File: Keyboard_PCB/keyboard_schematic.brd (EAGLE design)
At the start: 487.7 x 175.3 mm, 266 parts, among them IC1 LMV321M5, M2 KEYSWITCH-RGBSMDLED-ALPSMX-1U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, M3 KEYSWITCH-RGBSMDLED-ALPSMX-1U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, M4 KEYSWITCH-RGBSMDLED-ALPSMX-1U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, M5 KEYSWITCH-RGBSMDLED-ALPSMX-1U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, M6 KEYSWITCH-RGBSMDLED-ALPSMX-1U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, T1 BC846, Y2 CRYSTAL-GROUNDEDSMD-3.2X2.5

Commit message: Updated Schematics and boards
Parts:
- removed IC2: (no value), controller-micro_atmel_jd:QFN64
- removed U$2: PCB_USB_CDS_1, USB_pcb_connectors:USB_TYPE_C_DS_1
- added IC3: (no value), controller-micro_atmel_jd:TQFP64
- added J1: 1-2295018-2, 1-2295018-2:TE_1-2295018-2
- T1: value BC846 -> (none); device transistor:SOT23 -> transistor:SOT23-EBC
- moved C7 430.1 mm to (370.1, 134.4), flipped to the bottom, turned to 90 degrees
- moved R1 408.4 mm to (348.7, 132.3), flipped to the bottom, turned to 90 degrees
- moved C3 405.0 mm to (355.9, 134.4), flipped to the bottom, turned to 90 degrees
- moved S1 403.3 mm to (334.3, 160.3), flipped to the bottom, turned to 180 degrees
- moved C4 402.9 mm to (359.4, 134.4), flipped to the bottom, turned to 90 degrees
- moved R3 402.6 mm to (348.7, 145.0), flipped to the bottom, turned to 90 degrees
- moved R4 400.9 mm to (348.7, 149.1), flipped to the bottom, turned to 90 degrees
- moved C5 400.8 mm to (363.0, 134.4), flipped to the bottom, turned to 90 degrees
- moved C6 398.7 mm to (366.5, 134.4), flipped to the bottom, turned to 90 degrees
- moved C8 392.7 mm to (337.3, 137.7), flipped to the bottom
- moved R8 390.9 mm to (310.9, 158.5), flipped to the bottom, turned to 270 degrees
- moved T1 388.5 mm to (302.3, 156.0), flipped to the bottom, turned to 90 degrees
- moved R5 385.2 mm to (324.8, 158.0), flipped to the bottom, turned to 270 degrees
- moved R6 379.0 mm to (322.4, 158.0), flipped to the bottom, turned to 90 degrees
- moved C2 377.4 mm to (327.9, 124.7), flipped to the bottom, turned to 90 degrees
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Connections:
- removed net COL11: EQUAL2.ALPS1, EQUAL2.MX1, KP_9.ALPS1, KP_9.MX1, KP_ASTERISK.ALPS1, KP_ASTERISK.MX1, KP_DASH.ALPS1, KP_DASH.MX1, NEXTSONG.ALPS1, NEXTSONG.MX1, PAUSEPLAY.ALPS1, PAUSEPLAY.MX1
- removed net ROW1.1: DF1.C, DF11.C, DF3.C, DF5.C, DF7.C, DF9.C, DM6.C, DNEXTSONG1.C, DPAUSE.C, DPAUSEPLAY.C, DSCROLLLOCK.C, DVOLUMEUP.C
- removed net ROW1.2: DBACKSONG.C, DESC.C, DF10.C, DF12.C, DF2.C, DF4.C, DF6.C, DF8.C, DLOCK.C, DNEXTSONG.C, DPRTSC.C, DVOLUMNEDOWN.C
- removed net ROW2.1: D1.C, D3.C, D5.C, D7.C, D9.C, DBACKSPACE.C, DDASH.C, DHOME.C, DKP_DASH.C, DKP_SLASH.C, DM5.C
- removed net ROW2.2: D0.C, D2.C, D4.C, D6.C, D8.C, DEQUAL.C, DGRAVE.C, DINSERT.C, DKP_ASTERISK.C, DNUMLOCK.C, DPGUP.C, DUNDERSCORE.C
- removed net ROW3.1: DBACKSLASH.C, DE.C, DEND.C, DEQUAL2.C, DKP_8.C, DLBRACKET.C, DM4.C, DO.C, DQ.C, DT.C, DU.C
- removed net ROW3.2: DDELETE.C, DI.C, DKP_5.C, DKP_7.C, DKP_9.C, DP.C, DPGDN.C, DR.C, DRBRACKET.C, DTAB.C, DW.C, DY.C
- removed net ROW4.1: DA.C, DCTRL2.C, DD.C, DG.C, DJ.C, DKP_4.C, DKP_6.C, DKP_62.C, DL.C, DM3.C, DQUOTE.C
- removed net ROW4.2: DCAPSLOCK.C, DENTER.C, DENTER2.C, DF.C, DH.C, DK.C, DKP_52.C, DS.C, DSEMICOLON.C, DUP.C
- removed net ROW5.1: DB.C, DC.C, DKP_2.C, DLEFT.C, DM.C, DM2.C, DMENU.C, DPERIOD.C, DZ.C
- removed net ROW5.2: DCOMMA.C, DDELETE2.C, DKP_1.C, DKP_3.C, DN.C, DRIGHT.C, DSHIFT.C, DSHIFT2.C, DSLASH.C, DV.C, DX.C
- removed net ROW6.1: DALT.C, DALT2.C, DBACKSPACE_1.C, DCTRL.C, DDOWN.C, DKP_0.C, DKP_DEL.C, DM1.C, DSPACE.C, DWIN.C, DWIN2.C
- new net COL13: 0.ALPS1, 0.MX1, F10.ALPS1, F10.MX1, P.ALPS1, P.MX1, SEMICOLON.ALPS1, SEMICOLON.MX1, SLASH.ALPS1, SLASH.MX1, WIN2.ALPS1, WIN2.MX1
- new net COL14: DASH.ALPS1, DASH.MX1, F11.ALPS1, F11.MX1, LBRACKET.ALPS1, LBRACKET.MX1, MENU.ALPS1, MENU.MX1, QUOTE.ALPS1, QUOTE.MX1
- new net COL15: EQUAL.ALPS1, EQUAL.MX1, F12.ALPS1, F12.MX1, RBRACKET.ALPS1, RBRACKET.MX1
- new net COL16: VOLUMEUP.ALPS1, VOLUMEUP.MX1
- new net COL17: BACKSLASH.ALPS1, BACKSLASH.MX1, BACKSPACE.ALPS1, BACKSPACE.MX1, CTRL2.ALPS1, CTRL2.MX1, ENTER.ALPS1, ENTER.MX1, SHIFT2.ALPS1, SHIFT2.MX1, VOLUMNEDOWN.ALPS1, VOLUMNEDOWN.MX1
- new net COL18: DELETE.ALPS1, DELETE.MX1, INSERT.ALPS1, INSERT.MX1, LEFT.ALPS1, LEFT.MX1, PRTSC.ALPS1, PRTSC.MX1
- new net COL19: DOWN.ALPS1, DOWN.MX1, END.ALPS1, END.MX1, HOME.ALPS1, HOME.MX1, SCROLLLOCK.ALPS1, SCROLLLOCK.MX1, UP.ALPS1, UP.MX1
- new net COL20: PAUSE.ALPS1, PAUSE.MX1, PGDN.ALPS1, PGDN.MX1, PGUP.ALPS1, PGUP.MX1, RIGHT.ALPS1, RIGHT.MX1
- new net COL21: BACKSONG.ALPS1, BACKSONG.MX1, KP_0.ALPS1, KP_0.MX1, KP_1.ALPS1, KP_1.MX1, KP_4.ALPS1, KP_4.MX1, KP_7.ALPS1, KP_7.MX1, NUMLOCK.ALPS1, NUMLOCK.MX1
- new net COL22: KP_2.ALPS1, KP_2.MX1, KP_52.ALPS1, KP_52.MX1, KP_8.ALPS1, KP_8.MX1, KP_SLASH.ALPS1, KP_SLASH.MX1, PAUSEPLAY.ALPS1, PAUSEPLAY.MX1
- new net COL23: KP_3.ALPS1, KP_3.MX1, KP_6.ALPS1, KP_6.MX1, KP_9.ALPS1, KP_9.MX1, KP_ASTERISK.ALPS1, KP_ASTERISK.MX1, KP_DEL.ALPS1, KP_DEL.MX1, NEXTSONG.ALPS1, NEXTSONG.MX1
- new net COL24: ENTER2.ALPS1, ENTER2.MX1, EQUAL2.ALPS1, EQUAL2.MX1, KP_DASH.ALPS1, KP_DASH.MX1, RANDSONG.ALPS1, RANDSONG.MX1
- new net COL25: BACKSPACE_1.ALPS1, BACKSPACE_1.MX1, KP_5.ALPS1, KP_5.MX1, KP_62.ALPS1, KP_62.MX1, KP_DELETE2.ALPS1, KP_DELETE2.MX1, LOCK.ALPS1, LOCK.MX1, UNDERSCORE.ALPS1, UNDERSCORE.MX1
- new net LED1: M6.DIN
- new net LED2: M5.DIN
- new net LED3: M4.DIN
- new net LED4: M3.DIN
- new net LED5: M2.DIN
- new net LED6: CTRL1.DIN
- new net N$107: ESC.DIN, M6.DOUT
- new net N$118: ESC.DOUT, F1.DIN
- new net N$119: F1.DOUT, F2.DIN
- new net N$121: F2.DOUT, F3.DIN
- new net N$122: F3.DOUT, F4.DIN
- new net N$123: F4.DOUT, F5.DIN
- new net N$124: F5.DOUT, F6.DIN
- new net N$132: F6.DOUT, F7.DIN
- new net N$133: F7.DOUT, F8.DIN
- new net N$134: F8.DOUT, F9.DIN
- new net N$135: F10.DIN, F9.DOUT
- new net N$136: F10.DOUT, F11.DIN
- new net N$137: F11.DOUT, F12.DIN
- new net N$138: F12.DOUT, VOLUMEUP.DIN
- new net N$139: VOLUMEUP.DOUT, VOLUMNEDOWN.DIN
- new net N$140: PRTSC.DIN, VOLUMNEDOWN.DOUT
- new net N$141: PRTSC.DOUT, SCROLLLOCK.DIN
- new net N$142: PAUSE.DIN, SCROLLLOCK.DOUT
- new net N$143: BACKSONG.DIN, PAUSE.DOUT
- new net N$144: BACKSONG.DOUT, PAUSEPLAY.DIN
- new net N$145: NEXTSONG.DIN, PAUSEPLAY.DOUT
- new net N$146: NEXTSONG.DOUT, RANDSONG.DIN
- new net N$147: LOCK.DIN, RANDSONG.DOUT
- new net N$148: IC3.50
- new net N$149: GRAVE.DIN, M5.DOUT
- new net N$150: 1.DIN, GRAVE.DOUT
- new net N$151: 1.DOUT, 2.DIN
- new net N$152: 2.DOUT, 3.DIN
- new net N$153: 3.DOUT, 4.DIN
- new net N$154: 4.DOUT, 5.DIN
- new net N$155: 5.DOUT, 6.DIN
- new net N$156: 6.DOUT, 7.DIN
- new net N$157: 7.DOUT, 8.DIN
- new net N$158: 8.DOUT, 9.DIN
- new net N$159: 0.DIN, 9.DOUT
- new net N$160: 0.DOUT, DASH.DIN
- new net N$161: DASH.DOUT, EQUAL.DIN
- new net N$162: IC3.49
- new net N$163: BACKSPACE.R-, EQUAL.DOUT
- new net N$164: BACKSPACE.G-, INSERT.DIN
- new net N$165: HOME.DIN, INSERT.DOUT
- new net N$166: HOME.DOUT, PGUP.DIN
- new net N$167: NUMLOCK.DIN, PGUP.DOUT
- new net N$168: KP_SLASH.DIN, NUMLOCK.DOUT
- new net N$169: KP_ASTERISK.DIN, KP_SLASH.DOUT
- new net N$170: KP_ASTERISK.DOUT, KP_DASH.DIN
- new net N$171: KP_DASH.DOUT, UNDERSCORE.DIN
- new net N$172: M4.DOUT, TAB.DIN
- new net N$173: Q.DIN, TAB.DOUT
- new net N$174: Q.DOUT, W.DIN
- new net N$175: E.DIN, W.DOUT
- new net N$176: E.DOUT, R.DIN
- new net N$177: R.DOUT, T.DIN
- new net N$178: T.DOUT, Y.DIN
- new net N$179: U.DIN, Y.DOUT
- new net N$180: I.DIN, U.DOUT
- new net N$181: I.DOUT, O.DIN
- new net N$182: O.DOUT, P.DIN
- new net N$183: LBRACKET.DIN, P.DOUT
- new net N$184: LBRACKET.DOUT, RBRACKET.DIN
- new net N$185: BACKSLASH.DIN, RBRACKET.DOUT
- new net N$186: IC3.48
- new net N$187: BACKSLASH.DOUT, DELETE.DIN
- new net N$188: DELETE.DOUT, END.DIN
- new net N$189: END.DOUT, PGDN.DIN
- new net N$190: KP_7.DIN, PGDN.DOUT
- new net N$191: KP_7.DOUT, KP_8.DIN
- new net N$192: KP_8.DOUT, KP_9.DIN
- new net N$193: EQUAL2.DIN, KP_9.DOUT
- new net N$194: EQUAL2.DOUT, KP_5.DIN
- new net N$195: CAPSLOCK.DIN, M3.DOUT
- new net N$196: A.DIN, CAPSLOCK.DOUT
- new net N$197: A.DOUT, S.DIN
- new net N$198: D.DIN, S.DOUT
- new net N$199: D.DOUT, F.DIN
- new net N$200: F.DOUT, G.DIN
- new net N$201: G.DOUT, H.DIN
- new net N$202: H.DOUT, J.DIN
- new net N$203: J.DOUT, K.DIN
- new net N$204: K.DOUT, L.DIN
- new net N$205: L.DOUT, SEMICOLON.DIN
- new net N$206: QUOTE.DIN, SEMICOLON.DOUT
- new net N$207: ENTER.R-, QUOTE.DOUT
- new net N$208: ENTER.G-, KP_4.DIN
- new net N$209: ENTER2.DIN, KP_3.DOUT
- new net N$210: KP_4.DOUT, KP_52.DIN
- new net N$211: KP_52.DOUT, KP_6.DIN
- new net N$212: KP_6.DOUT, KP_62.DIN
- new net N$213: IC3.47
- new net N$214: M2.DOUT, SHIFT.R-
- new net N$215: SHIFT.G-, Z.DIN
- new net N$216: X.DIN, Z.DOUT
- new net N$217: C.DIN, X.DOUT
- new net N$218: C.DOUT, V.DIN
- new net N$219: B.DIN, V.DOUT
- new net N$220: B.DOUT, N.DIN
- new net N$221: M.DIN, N.DOUT
- new net N$222: COMMA.DIN, M.DOUT
- new net N$223: COMMA.DOUT, PERIOD.DIN
- new net N$224: PERIOD.DOUT, SLASH.DIN
- new net N$225: SHIFT2.R-, SLASH.DOUT
- new net N$226: IC3.46
- new net N$227: KP_1.DOUT, KP_2.DIN
- new net N$228: KP_2.DOUT, KP_3.DIN
- new net N$229: ENTER2.DOUT, KP_DELETE2.DIN
- new net N$230: KP_1.DIN, SHIFT2.G-
- new net N$231: IC3.45
- new net N$232: CTRL.DIN, CTRL1.DOUT
- new net N$233: CTRL.DOUT, WIN.DIN
- new net N$234: ALT.DIN, WIN.DOUT
- new net N$235: ALT.DOUT, SPACE.R-
- new net N$236: IC3.44
- new net N$238: ALT2.DIN, SPACE.G-
- new net N$239: J1.B9
- new net N$242: ALT2.DOUT, WIN2.DIN
- new net N$243: MENU.DIN, WIN2.DOUT
- new net N$245: CTRL2.DIN, MENU.DOUT
- new net N$246: CTRL2.DOUT, LEFT.DIN
- new net N$247: KP_0.R-
- new net N$248: KP_0.G-, KP_DEL.DIN
- new net N$249: BACKSPACE_1.DIN, KP_DEL.DOUT
- new net N$250: DOWN.DIN, LEFT.DOUT
- new net N$251: DOWN.DOUT, RIGHT.DIN
- new net N$252: RIGHT.DOUT
- new net ROW1: DBACKSONG.C, DESC.C, DF1.C, DF10.C, DF11.C, DF12.C, DF2.C, DF3.C, DF4.C, DF5.C, DF6.C, DF7.C, DF8.C, DF9.C, DLOCK.C, DM6.C, DNEXTSONG.C, DNEXTSONG1.C, DPAUSE.C, DPAUSEPLAY.C, DPRTSC.C, DSCROLLLOCK.C, DVOLUMEUP.C, DVOLUMNEDOWN.C
- new net ROW2: D0.C, D1.C, D2.C, D3.C, D4.C, D5.C, D6.C, D7.C, D8.C, D9.C, DBACKSPACE.C, DDASH.C, DEQUAL.C, DGRAVE.C, DHOME.C, DINSERT.C, DKP_ASTERISK.C, DKP_DASH.C, DKP_SLASH.C, DM5.C, DNUMLOCK.C, DPGUP.C, DUNDERSCORE.C
- new net ROW3: DBACKSLASH.C, DDELETE.C, DE.C, DEND.C, DEQUAL2.C, DI.C, DKP_5.C, DKP_7.C, DKP_8.C, DKP_9.C, DLBRACKET.C, DM4.C, DO.C, DP.C, DPGDN.C, DQ.C, DR.C, DRBRACKET.C, DT.C, DTAB.C, DU.C, DW.C, DY.C
- new net ROW4: DA.C, DCAPSLOCK.C, DD.C, DENTER.C, DF.C, DG.C, DH.C, DJ.C, DK.C, DKP_4.C, DKP_52.C, DKP_6.C, DKP_62.C, DL.C, DM3.C, DQUOTE.C, DS.C, DSEMICOLON.C
- new net ROW5: DB.C, DC.C, DCOMMA.C, DDELETE2.C, DENTER2.C, DKP_1.C, DKP_2.C, DKP_3.C, DM.C, DM2.C, DN.C, DPERIOD.C, DSHIFT.C, DSHIFT2.C, DSLASH.C, DUP.C, DV.C, DX.C, DZ.C
- new net ROW6: DALT.C, DALT2.C, DBACKSPACE_1.C, DCTRL2.C, DDOWN.C, DKP_0.C, DKP_DEL.C, DLEFT.C, DM1.C, DMENU.C, DRIGHT.C, DSPACE.C, DWIN.C, DWIN2.C
- net +5V: now also IC3.21, IC3.52, IC3.62, IC3.64, J1.A4, J1.A9, J1.B4, T1.C; no longer IC2.21, IC2.52, IC2.62, IC2.64, T1.3, U$2.A4, U$2.A9, U$2.B4, U$2.B9
- net CC1: now also IC1.1, J1.A5, R6.2; no longer R5.1, U$2.A5
- net CC2: now also J1.B5, R5.1; no longer IC1.1, R6.2, U$2.B5
- net COL1: no longer CAPSLOCK.ALPS1, CAPSLOCK.MX1, ESC.ALPS1, ESC.MX1, GRAVE.ALPS1, GRAVE.MX1, SHIFT.ALPS1, SHIFT.MX1, TAB.ALPS1, TAB.MX1
- net COL10: now also 8.ALPS1, 8.MX1, COMMA.ALPS1, COMMA.MX1, F8.ALPS1, F8.MX1, I.ALPS1, I.MX1, K.ALPS1, K.MX1; no longer BACKSONG.ALPS1, BACKSONG.MX1, ENTER2.ALPS1, ENTER2.MX1, KP_3.ALPS1, KP_3.MX1, KP_6.ALPS1, KP_6.MX1, KP_7.ALPS1, KP_7.MX1, KP_8.ALPS1, KP_8.MX1, KP_DEL.ALPS1, KP_DEL.MX1, KP_SLASH.ALPS1, KP_SLASH.MX1, NUMLOCK.ALPS1, NUMLOCK.MX1, PAUSE.ALPS1, PAUSE.MX1
- net COL12: now also 9.ALPS1, 9.MX1, ALT2.ALPS1, ALT2.MX1, F9.ALPS1, F9.MX1, L.ALPS1, L.MX1, O.ALPS1, O.MX1, PERIOD.ALPS1, PERIOD.MX1; no longer BACKSPACE_1.ALPS1, BACKSPACE_1.MX1, KP_5.ALPS1, KP_5.MX1, KP_62.ALPS1, KP_62.MX1, KP_DELETE2.ALPS1, KP_DELETE2.MX1, LOCK.ALPS1, LOCK.MX1, RANDSONG.ALPS1, RANDSONG.MX1, UNDERSCORE.ALPS1, UNDERSCORE.MX1
- net COL2: now also CAPSLOCK.ALPS1, CAPSLOCK.MX1, ESC.ALPS1, ESC.MX1, GRAVE.ALPS1, GRAVE.MX1, SHIFT.ALPS1, SHIFT.MX1, TAB.ALPS1, TAB.MX1; no longer 1.ALPS1, 1.MX1, 2.ALPS1, 2.MX1, A.ALPS1, A.MX1, F1.ALPS1, F1.MX1, F2.ALPS1, F2.MX1, Q.ALPS1, Q.MX1, S.ALPS1, S.MX1, W.ALPS1, W.MX1, X.ALPS1, X.MX1, Z.ALPS1, Z.MX1
- net COL3: now also 1.ALPS1, 1.MX1, A.ALPS1, A.MX1, F1.ALPS1, F1.MX1, Q.ALPS1, Q.MX1, Z.ALPS1, Z.MX1; no longer 3.ALPS1, 3.MX1, 4.ALPS1, 4.MX1, C.ALPS1, C.MX1, D.ALPS1, D.MX1, E.ALPS1, E.MX1, F.ALPS1, F.MX1, F3.ALPS1, F3.MX1, F4.ALPS1, F4.MX1, R.ALPS1, R.MX1, V.ALPS1, V.MX1
- net COL4: now also 2.ALPS1, 2.MX1, F2.ALPS1, F2.MX1, S.ALPS1, S.MX1, W.ALPS1, W.MX1, X.ALPS1, X.MX1; no longer 5.ALPS1, 5.MX1, 6.ALPS1, 6.MX1, B.ALPS1, B.MX1, F5.ALPS1, F5.MX1, F6.ALPS1, F6.MX1, G.ALPS1, G.MX1, H.ALPS1, H.MX1, N.ALPS1, N.MX1, T.ALPS1, T.MX1, Y.ALPS1, Y.MX1
- net COL5: now also 3.ALPS1, 3.MX1, C.ALPS1, C.MX1, D.ALPS1, D.MX1, E.ALPS1, E.MX1, F3.ALPS1, F3.MX1; no longer 7.ALPS1, 7.MX1, 8.ALPS1, 8.MX1, COMMA.ALPS1, COMMA.MX1, F7.ALPS1, F7.MX1, F8.ALPS1, F8.MX1, I.ALPS1, I.MX1, J.ALPS1, J.MX1, K.ALPS1, K.MX1, M.ALPS1, M.MX1, SPACE.ALPS1, SPACE.MX1, U.ALPS1, U.MX1
- net COL6: now also 4.ALPS1, 4.MX1, F.ALPS1, F.MX1, F4.ALPS1, F4.MX1, R.ALPS1, R.MX1, V.ALPS1, V.MX1; no longer 0.ALPS1, 0.MX1, 9.ALPS1, 9.MX1, ALT2.ALPS1, ALT2.MX1, F10.ALPS1, F10.MX1, F9.ALPS1, F9.MX1, L.ALPS1, L.MX1, O.ALPS1, O.MX1, P.ALPS1, P.MX1, PERIOD.ALPS1, PERIOD.MX1, SEMICOLON.ALPS1, SEMICOLON.MX1, SLASH.ALPS1, SLASH.MX1
- net COL7: now also 5.ALPS1, 5.MX1, B.ALPS1, B.MX1, F5.ALPS1, F5.MX1, G.ALPS1, G.MX1, SPACE.ALPS1, SPACE.MX1, T.ALPS1, T.MX1; no longer DASH.ALPS1, DASH.MX1, ENTER.ALPS1, ENTER.MX1, EQUAL.ALPS1, EQUAL.MX1, F11.ALPS1, F11.MX1, F12.ALPS1, F12.MX1, LBRACKET.ALPS1, LBRACKET.MX1, MENU.ALPS1, MENU.MX1, QUOTE.ALPS1, QUOTE.MX1, RBRACKET.ALPS1, RBRACKET.MX1, SHIFT2.ALPS1, SHIFT2.MX1, WIN2.ALPS1, WIN2.MX1
- net COL8: now also 6.ALPS1, 6.MX1, F6.ALPS1, F6.MX1, H.ALPS1, H.MX1, N.ALPS1, N.MX1, Y.ALPS1, Y.MX1; no longer BACKSLASH.ALPS1, BACKSLASH.MX1, BACKSPACE.ALPS1, BACKSPACE.MX1, CTRL2.ALPS1, CTRL2.MX1, DELETE.ALPS1, DELETE.MX1, DOWN.ALPS1, DOWN.MX1, INSERT.ALPS1, INSERT.MX1, LEFT.ALPS1, LEFT.MX1, RIGHT.ALPS1, RIGHT.MX1, UP.ALPS1, UP.MX1, VOLUMEUP.ALPS1, VOLUMEUP.MX1, VOLUMNEDOWN.ALPS1, VOLUMNEDOWN.MX1
- net COL9: now also 7.ALPS1, 7.MX1, F7.ALPS1, F7.MX1, J.ALPS1, J.MX1, M.ALPS1, M.MX1, U.ALPS1, U.MX1; no longer END.ALPS1, END.MX1, HOME.ALPS1, HOME.MX1, KP_0.ALPS1, KP_0.MX1, KP_1.ALPS1, KP_1.MX1, KP_2.ALPS1, KP_2.MX1, KP_4.ALPS1, KP_4.MX1, KP_52.ALPS1, KP_52.MX1, PGDN.ALPS1, PGDN.MX1, PGUP.ALPS1, PGUP.MX1, PRTSC.ALPS1, PRTSC.MX1, SCROLLLOCK.ALPS1, SCROLLLOCK.MX1
- net D+32U: now also IC3.5; no longer IC2.5
- net D+USB: now also J1.B6; no longer U$2.A6
- net D-32U4: now also IC3.4; no longer IC2.4
- net D-USB: now also J1.B7; no longer U$2.A7
- net GND: now also IC3.22, IC3.53, IC3.6, IC3.63, J1.A1, J1.A12, J1.B1, J1.B12, J1.P1_1, J1.P1_2, J1.P2_1, J1.P2_2, J1.P4, J1.P5; no longer IC2.22, IC2.53, IC2.6, IC2.63, U$2.A1, U$2.A12, U$2.B1, U$2.B12
- net LED_VCC: now also T1.E; no longer T1.2
- net N$102: now also IC3.51; no longer CTRL.ALPS2, CTRL.MX2, DCTRL.A
- net N$117: now also T1.B; no longer T1.1
- net PE2: now also IC3.43; no longer IC2.43
- net RESET: now also IC3.20; no longer IC2.20
- net UCAP: now also IC3.7; no longer IC2.7
- net UVCC: now also IC3.3; no longer IC2.3
- net XTAL1: now also IC3.24; no longer IC2.24
- net XTAL2: now also IC3.23; no longer IC2.23
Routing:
- net GND: track 0.00 -> 110.0 mm
- net VCC: track 0.00 -> 17.6 mm
- net +5V: track 0.00 -> 14.4 mm, vias 0 -> 2
- net XTAL2: track 0.00 -> 10.0 mm
- net UCAP: track 0.00 -> 5.84 mm
- net N$116: track 0.00 -> 5.39 mm
- net PE2: track 0.00 -> 4.02 mm
- net XTAL1: track 0.00 -> 3.81 mm
- net N$117: track 0.00 -> 1.27 mm

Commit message: Updated board
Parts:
- moved C7 40.7 mm to (330.9, 145.4), turned to 270 degrees
- moved C6 35.3 mm to (333.0, 145.4), turned to 270 degrees
- moved C5 30.1 mm to (335.0, 145.4), turned to 270 degrees
- moved C4 24.9 mm to (337.0, 145.4), turned to 270 degrees
- moved C3 20.1 mm to (339.1, 145.4), turned to 270 degrees
- moved T1 7.43 mm to (309.1, 158.9)
- moved R7 6.84 mm to (313.4, 160.8)
- moved R8 6.84 mm to (313.4, 164.8)
- moved IC1 6.84 mm to (309.1, 162.3)
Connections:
- net +5V: now also C3.1, C4.1, C5.1, C6.1, C7.1
- net VCC: no longer C3.1, C4.1, C5.1, C6.1, C7.1
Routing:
- net +5V: track 14.4 -> 76.8 mm, vias 2 -> 4
- net VCC: track 17.6 -> 0.00 mm
- net GND: track 110.0 -> 102.8 mm
- net CC1: track 0.00 -> 2.01 mm

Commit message: Updated Board
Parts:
- removed IC1: LMV321M5, linear:SOT23-5
- removed R7: 475, rcl:M0805
- removed R8: 150, rcl:M0805
- removed T1: (no value), transistor:SOT23-EBC
- moved R3 25.1 mm to (324.6, 151.9), turned to 270 degrees
- moved R4 22.3 mm to (326.6, 151.9), turned to 270 degrees
- moved C4 21.3 mm to (331.4, 124.8)
- moved R1 17.0 mm to (333.5, 124.8), turned to 270 degrees
- moved C6 14.8 mm to (318.5, 148.5), turned to 90 degrees
- moved C5 9.29 mm to (335.5, 136.1), turned to 180 degrees
- moved R6 8.53 mm to (314.3, 160.8)
- moved C3 8.39 mm to (330.7, 145.1)
- moved R5 6.41 mm to (322.6, 151.9)
- moved J1 5.85 mm to (323.3, 159.8)
- moved S1 5.85 mm to (334.5, 154.4)
- moved C7 4.73 mm to (335.5, 144.3), turned to 180 degrees
- moved C8 1.85 mm to (335.5, 138.2)
- moved R2 0.76 mm to (310.9, 138.7)
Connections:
- removed net CC1: IC1.1, J1.A5, R6.2
- removed net CC2: J1.B5, R5.1
- removed net LED_VCC: T1.E
- removed net N$102: IC3.51
- removed net N$116: IC1.3, R7.1, R8.2
- removed net N$117: IC1.4, T1.B
- removed net N$148: IC3.50
- removed net N$162: IC3.49
- removed net N$186: IC3.48
- removed net N$213: IC3.47
- removed net N$226: IC3.46
- removed net N$231: IC3.45
- removed net N$236: IC3.44
- removed net UVCC: IC3.3
- removed net VCC: R1.1
- new net N$237: J1.A5, R5.1
- new net N$255: J1.B5, R6.2
- net +5V: now also IC3.3, IC3.8, J1.B9, R1.1; no longer IC1.5, J1.A9, R7.2, T1.C
- net D+USB: now also J1.A6; no longer J1.B6
- net D-USB: now also J1.A7; no longer J1.B7
- net GND: no longer IC1.2, R8.1
- net N$239: now also J1.A9; no longer J1.B9
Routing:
- net RESET: track 0.00 -> 45.2 mm
- net GND: track 102.8 -> 147.9 mm, vias 0 -> 4
- net D+32U: track 0.00 -> 28.1 mm, vias 0 -> 2
- net D-32U4: track 0.00 -> 24.1 mm
- net N$255: track 0.00 -> 12.9 mm, vias 0 -> 2
- net +5V: track 76.8 -> 82.4 mm, vias 4 -> 7
- net N$116: track 5.40 -> 0.00 mm
- net D-USB: track 0.00 -> 4.22 mm
- net D+USB: track 0.00 -> 2.87 mm
- net N$237: track 0.00 -> 2.26 mm
- net CC1: track 2.01 -> 0.00 mm
- net XTAL2: track 10.0 -> 12.0 mm
- net XTAL1: track 3.81 -> 5.72 mm
- net UCAP: track 5.84 -> 4.13 mm
- net N$117: track 1.65 -> 0.00 mm
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
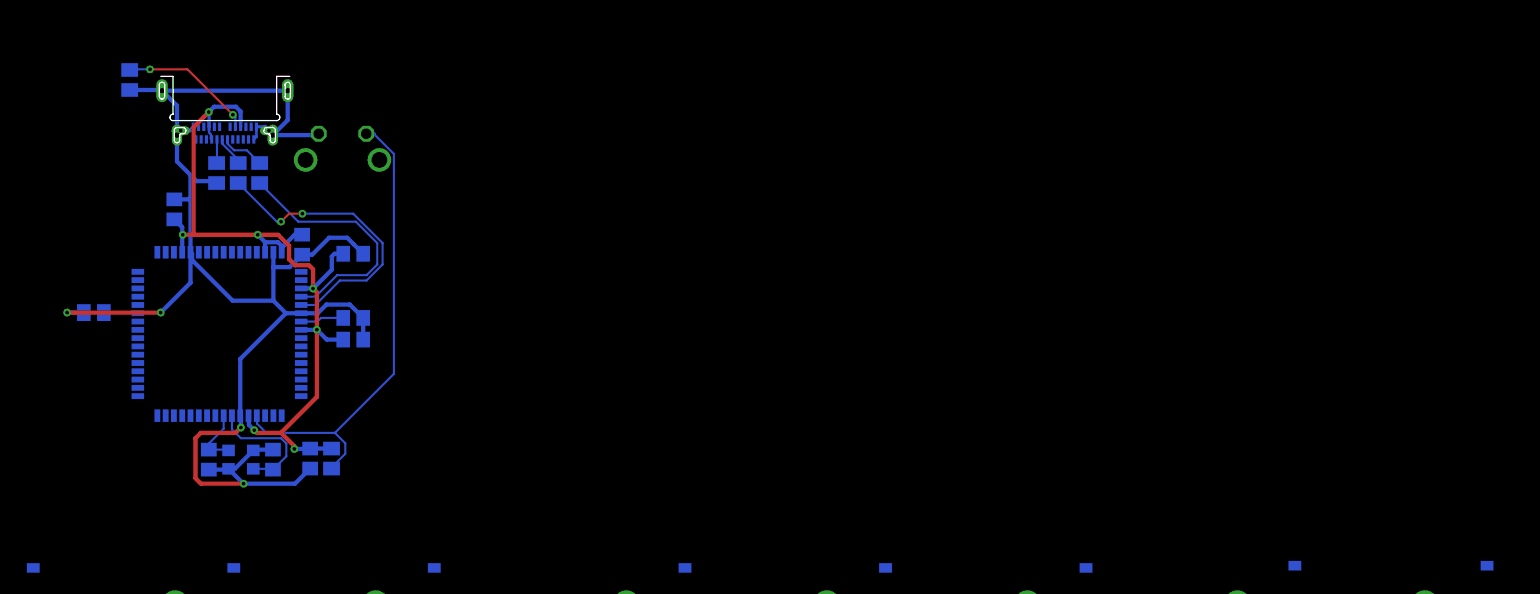
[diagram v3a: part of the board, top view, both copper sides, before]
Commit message: Updated Schematic and rerouted board
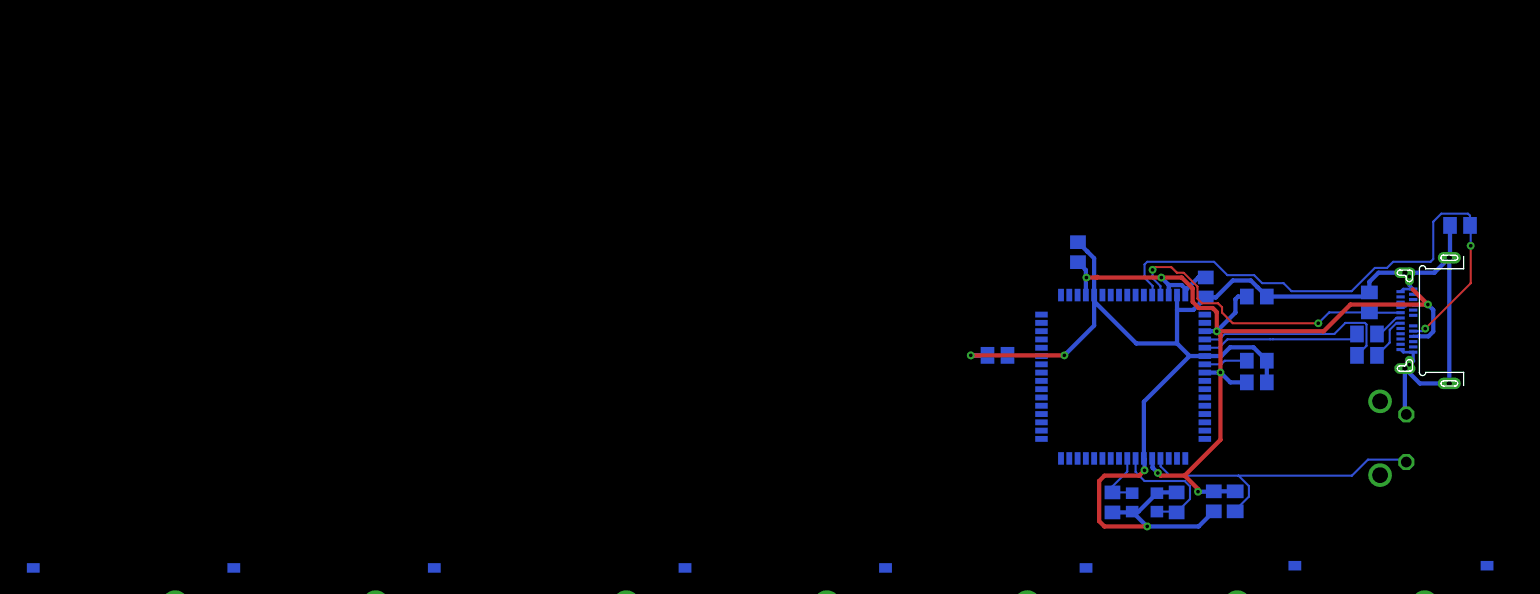
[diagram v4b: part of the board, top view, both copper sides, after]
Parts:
- moved R6 127.1 mm to (440.7, 147.0), turned to 180 degrees
- moved J1 118.4 mm to (439.7, 137.9), turned to 270 degrees
- moved R5 110.2 mm to (432.1, 139.6), turned to 90 degrees
- moved R3 108.3 mm to (431.9, 136.7), turned to 0 degrees
- moved R4 106.6 mm to (431.9, 134.6), turned to 0 degrees
- moved S1 103.6 mm to (434.3, 126.7), turned to 270 degrees
- moved C1 85.9 mm to (407.7, 120.7)
- moved C2 85.9 mm to (413.8, 120.7)
- moved C3 85.9 mm to (416.5, 141.1)
- moved C4 85.9 mm to (417.3, 120.8)
- moved C5 85.9 mm to (421.4, 132.1)
- moved C7 85.9 mm to (421.4, 140.2)
- moved C8 85.9 mm to (421.4, 134.1)
- moved Y2 85.9 mm to (410.7, 120.7)
- moved C6 85.9 mm to (404.4, 144.4)
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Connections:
- removed net N$237: J1.A5, R5.1
- removed net N$255: J1.B5, R6.2
- new net CC1: IC3.61, J1.A5, R5.1
- new net CC2: IC3.60, J1.B5, R6.2
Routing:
- net CC2: track 0.00 -> 54.5 mm, vias 0 -> 2
- net CC1: track 0.00 -> 30.0 mm, vias 0 -> 2
- net RESET: track 45.2 -> 29.5 mm
- net D+32U: track 28.1 -> 15.0 mm, vias 2 -> 0
- net N$255: track 12.9 -> 0.00 mm, vias 2 -> 0
- net +5V: track 82.4 -> 93.4 mm
- net D-32U4: track 24.1 -> 19.4 mm
- net GND: track 147.9 -> 151.9 mm
- net N$237: track 2.26 -> 0.00 mm
